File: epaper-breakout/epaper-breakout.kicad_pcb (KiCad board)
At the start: 2 copper layers, 81.3 x 69.8 mm, 63 parts, among them J1 ED097OC4, J2 USB_B_Micro, J3 Conn_01x10, Q1 IRLML6402, SW1 RESET, SW2 BOOT, U1 LT1086-3.3, U2 LT1945, U3 L7915, U4 L7815, U5 ESP32-WROOM-32, U6 CH330N, U7 LM358

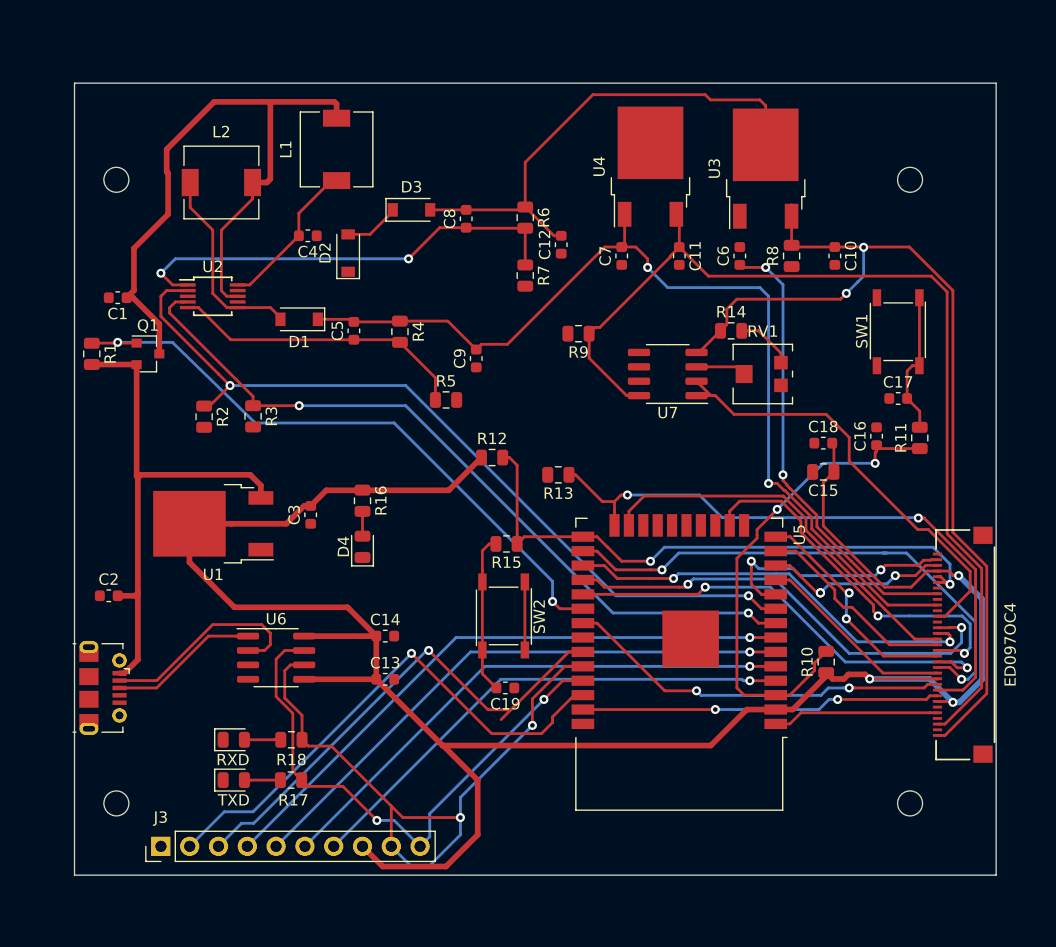
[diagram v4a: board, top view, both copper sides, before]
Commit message: copper pour and ground connections
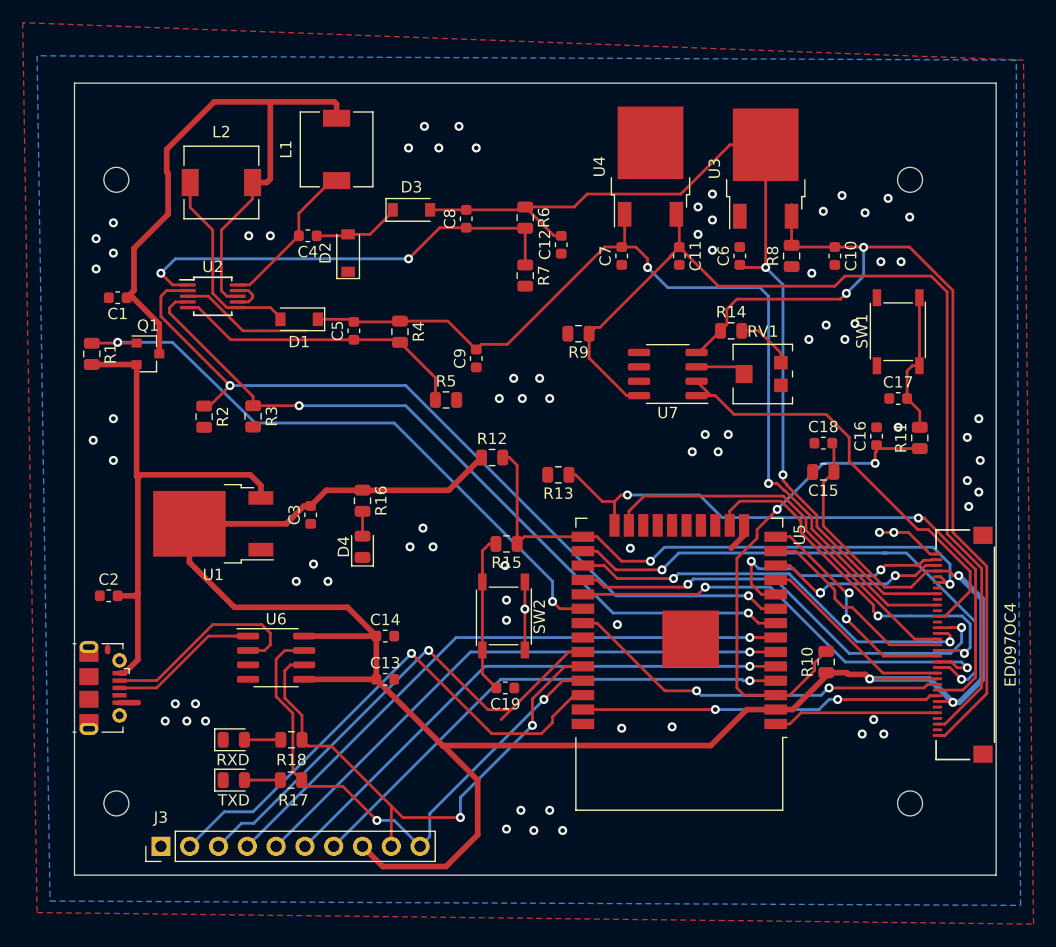
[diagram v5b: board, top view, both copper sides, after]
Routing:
- net GND: track 20.7 -> 45.7 mm, vias 0 -> 76
- net /USB_TXD: track 57.3 -> 47.8 mm
- net /-20V: track 84.4 -> 87.2 mm
- net Net-(C4-Pad1): track 4.92 -> 7.74 mm
- net /15V: track 88.7 -> 89.5 mm
- added copper zone on B.Cu, net GND
- added copper zone on F.Cu, net GND

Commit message: add silk hints
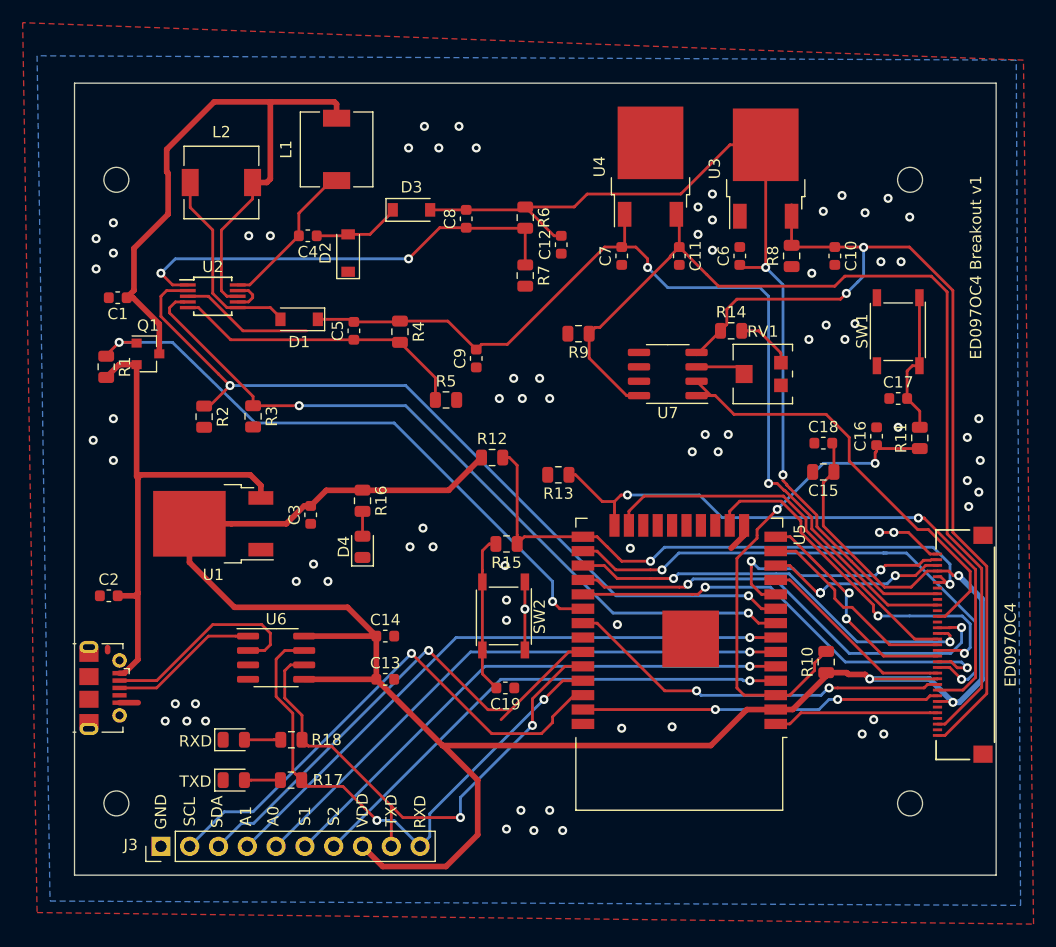
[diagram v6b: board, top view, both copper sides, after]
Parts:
- moved R1 1.71 mm to (54.1, -103.5)
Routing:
- net /5V: track 46.5 -> 45.7 mm
- net /~SMPS_CTRL: track 55.8 -> 55.1 mm
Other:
- board text added: "A0"
- board text added: "A1"
- board text added: "ED097OC4 Breakout v1"
- board text added: "GND"
- board text added: "RXD"
- board text added: "S1"
- board text added: "S2"
- board text added: "SCL"
- board text added: "SDA"
- board text added: "TXD"
- board text added: "VDD"
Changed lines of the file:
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@@
   (general
     (thickness 1.6)
-    (drawings 4)
-    (tracks 780)
+    (drawings 38)
+    (tracks 783)
     (zones 0)
     (modules 63)
@@
     (tags resistor)
     (attr smd)
-    (fp_text reference R18 (at 0 1.778) (layer F.SilkS)
+    (fp_text reference R18 (at 3.0965 0) (layer F.SilkS)
       (effects (font (size 1 1) (thickness 0.15)))
     )
@@
     (tags resistor)
     (attr smd)
-    (fp_text reference R17 (at 0.2055 1.778) (layer F.SilkS)
+    (fp_text reference R17 (at 3.2535 0) (layer F.SilkS)
       (effects (font (size 1 1) (thickness 0.15)))
     )
@@
   )
   (module Resistor_SMD:R_0805_2012Metric (layer F.Cu)
-    (at 52.832 -104.648 270)
+    (at 54.102 -103.505 270)
     (descr "Resistor SMD 0805 (2012 Metric), square (rectangular) end terminal, IPC_7351 nominal, (Body size source: https://docs.google.com/spreadsheets/d/1BsfQQcO9C6DZCsRaXUlFlo91Tg2WpOkGARC1WS5S8t0/edit?usp=sharing), generated with kicad-footprint-generator")
     (tags resistor)
@@
     (descr "Through hole straight pin header, 1x10, 2.54mm pitch, single row")
     (tags "Through hole pin header THT 1x10 2.54mm single row")
-    (fp_text reference J3 (at 2.54 0 180) (layer F.SilkS)
+    (fp_text reference J3 (at 0.127 -2.667 180) (layer F.SilkS)
       (effects (font (size 1 1) (thickness 0.15)))
     )
@@
     (tags diode)
     (attr smd)
-    (fp_text reference RXD (at -0.0785 1.778) (layer F.SilkS)
+    (fp_text reference RXD (at -3.3805 0.127) (layer F.SilkS)
       (effects (font (size 1 1) (thickness 0.15)))
     )
@@
     (tags diode)
     (attr smd)
-    (fp_text reference TXD (at 0 1.778) (layer F.SilkS)
+    (fp_text reference TXD (at -3.3805 0.127) (layer F.SilkS)
       (effects (font (size 1 1) (thickness 0.15)))
     )
@@
     )
   )
+  (gr_text RXD (at 81.788 -64.262 90) (layer F.SilkS)
+    (effects (font (size 1 1) (thickness 0.15)))
+  )
+  (gr_text TXD (at 79.248 -64.389 90) (layer F.SilkS)
+    (effects (font (size 1 1) (thickness 0.15)))
+  )
+  (gr_text VDD (at 76.708 -64.389 90) (layer F.SilkS)
+    (effects (font (size 1 1) (thickness 0.15)))
+  )
+  (gr_text S2 (at 74.168 -63.881 90) (layer F.SilkS)
+    (effects (font (size 1 1) (thickness 0.15)))
+  )
+  (gr_text S1 (at 71.628 -63.881 90) (layer F.SilkS)
+    (effects (font (size 1 1) (thickness 0.15)))
+  )
+  (gr_text A0 (at 68.834 -63.881 90) (layer F.SilkS)
+    (effects (font (size 1 1) (thickness 0.15)))
+  )
+  (gr_text A1 (at 66.421 -63.881 90) (layer F.SilkS)
+    (effects (font (size 1 1) (thickness 0.15)))
+  )
+  (gr_text SDA (at 63.881 -64.262 90) (layer F.SilkS)
+    (effects (font (size 1 1) (thickness 0.15)))
+  )
+  (gr_text SCL (at 61.468 -64.262 90) (layer F.SilkS)
+    (effects (font (size 1 1) (thickness 0.15)))
+  )
+  (gr_text "GND\n" (at 58.928 -64.262 90) (layer F.SilkS)
+    (effects (font (size 1 1) (thickness 0.15)))
+  )
+  (gr_line (start 65.532 -83.058) (end 59.944 -82.55) (layer B.SilkS) (width 0.12))
+  (gr_line (start 65.532 -83.058) (end 72.39 -82.55) (layer B.SilkS) (width 0.12))
+  (gr_line (start 65.024 -90.932) (end 65.151 -92.329) (layer B.SilkS) (width 0.12))
+  (gr_line (start 62.357 -90.805) (end 60.325 -90.551) (layer B.SilkS) (width 0.12))
+  (gr_line (start 60.706 -92.456) (end 59.055 -92.583) (layer B.SilkS) (width 0.12))
+  (gr_line (start 62.357 -90.805) (end 60.706 -92.456) (layer B.SilkS) (width 0.12))
+  (gr_line (start 69.723 -91.313) (end 70.231 -92.71) (layer B.SilkS) (width 0.12))
+  (gr_line (start 67.183 -90.424) (end 69.723 -91.313) (layer B.SilkS) (width 0.12))
+  (gr_line (start 68.834 -92.329) (end 69.977 -94.996) (layer B.SilkS) (width 0.12))
+  (gr_line (start 65.405 -93.218) (end 64.516 -94.996) (layer B.SilkS) (width 0.12))
+  (gr_line (start 63.246 -93.091) (end 63.119 -95.631) (layer B.SilkS) (width 0.12))
+  (gr_line (start 65.024 -90.932) (end 63.246 -93.091) (layer B.SilkS) (width 0.12))
+  (gr_line (start 65.659 -87.884) (end 65.024 -90.932) (layer B.SilkS) (width 0.12))
+  (gr_line (start 68.834 -92.329) (end 67.945 -94.361) (layer B.SilkS) (width 0.12))
+  (gr_line (start 67.183 -90.297) (end 68.834 -92.329) (layer B.SilkS) (width 0.12))
+  (gr_line (start 65.405 -93.218) (end 66.421 -95.25) (layer B.SilkS) (width 0.12))
+  (gr_line (start 67.183 -90.297) (end 65.405 -93.218) (layer B.SilkS) (width 0.12))
+  (gr_line (start 65.659 -87.884) (end 67.183 -90.297) (layer B.SilkS) (width 0.12))
+  (gr_line (start 61.722 -94.361) (end 61.087 -96.393) (layer B.SilkS) (width 0.12))
+  (gr_line (start 61.722 -94.361) (end 62.992 -97.409) (layer B.SilkS) (width 0.12))
+  (gr_line (start 62.357 -90.805) (end 61.722 -94.361) (layer B.SilkS) (width 0.12))
+  (gr_line (start 65.659 -87.884) (end 62.357 -90.805) (layer B.SilkS) (width 0.12))
+  (gr_line (start 65.532 -83.058) (end 65.659 -87.884) (layer B.SilkS) (width 0.12))
+  (gr_text "ED097OC4 Breakout v1" (at 130.81 -112.268 90) (layer F.SilkS)
+    (effects (font (size 1 1) (thickness 0.15)))
+  )
   (gr_line (start 51.308 -128.524) (end 132.588 -128.524) (layer Edge.Cuts) (width 0.1))
   (gr_line (start 51.308 -58.674) (end 51.308 -128.524) (layer Edge.Cuts) (width 0.1))
   (gr_line (start 132.588 -58.674) (end 51.308 -58.674) (layer Edge.Cuts) (width 0.1))
   (gr_line (start 132.588 -128.524) (end 132.588 -58.674) (layer Edge.Cuts) (width 0.1))
-  (segment (start 54.229 -78.74) (end 54.229 -78.385) (width 0.5) (layer F.Cu) (net 0) (status 1000000))
+  (segment (start 54.229 -78.74) (end 54.229 -78.385) (width 0.5) (layer F.Cu) (net 0))
   (segment (start 126.7627 -72.994002) (end 127.4191 -72.994002) (width 0.25) (layer F.Cu) (net 1))
   (segment (start 114.398 -72.009) (end 115.383002 -72.994002) (width 0.25) (layer F.Cu) (net 1))
@@
   (segment (start 56.896 -93.726) (end 57.15 -93.98) (width 0.5) (layer F.Cu) (net 3))
   (segment (start 56.7725 -103.7105) (end 56.785 -103.698) (width 0.5) (layer F.Cu) (net 3))
-  (segment (start 52.832 -103.7105) (end 56.7725 -103.7105) (width 0.5) (layer F.Cu) (net 3))
   (segment (start 56.785 -93.837) (end 56.785 -103.698) (width 0.5) (layer F.Cu) (net 3))
   (segment (start 56.896 -93.726) (end 56.785 -93.837) (width 0.5) (layer F.Cu) (net 3))
@@
   (segment (start 56.896 -77.677) (end 56.896 -83.566) (width 0.5) (layer F.Cu) (net 3))
   (segment (start 56.896 -83.566) (end 56.896 -93.726) (width 0.5) (layer F.Cu) (net 3))
+  (segment (start 55.2325 -103.698) (end 54.102 -102.5675) (width 0.5) (layer F.Cu) (net 3))
+  (segment (start 56.785 -103.698) (end 55.2325 -103.698) (width 0.5) (layer F.Cu) (net 3))
   (segment (start 127.401362 -75.976263) (end 127.4191 -75.994001) (width 0.25) (layer F.Cu) (net 4))
   (segment (start 126.51641 -85.494) (end 125.09641 -84.074) (width 0.25) (layer F.Cu) (net 4))
@@
   (segment (start 67.252998 -98.552) (end 59.944 -105.664) (width 0.25) (layer B.Cu) (net 56))
   (segment (start 79.502 -98.552) (end 67.252998 -98.552) (width 0.25) (layer B.Cu) (net 56))
-  (via (at 55.118 -105.664) (size 0.8) (drill 0.4) (layers F.Cu B.Cu) (net 56))
+  (via (at 55.245 -105.664) (size 0.8) (drill 0.4) (layers F.Cu B.Cu) (net 56))
   (segment (start 56.851 -105.664) (end 56.785 -105.598) (width 0.25) (layer F.Cu) (net 56))
-  (segment (start 52.8445 -105.598) (end 52.832 -105.5855) (width 0.25) (layer F.Cu) (net 56))
-  (segment (start 56.785 -105.598) (end 52.8445 -105.598) (width 0.25) (layer F.Cu) (net 56))
   (segment (start 59.944 -105.664) (end 55.118 -105.664) (width 0.25) (layer B.Cu) (net 56))
+  (segment (start 54.102 -104.521) (end 55.245 -105.664) (width 0.25) (layer F.Cu) (net 56))
+  (segment (start 54.102 -104.4425) (end 54.102 -104.521) (width 0.25) (layer F.Cu) (net 56))
+  (segment (start 56.719 -105.664) (end 56.785 -105.598) (width 0.25) (layer F.Cu) (net 56))
+  (segment (start 55.245 -105.664) (end 56.719 -105.664) (width 0.25) (layer F.Cu) (net 56))
   (segment (start 111.898 -82.169) (end 110.755 -83.312) (width 0.25) (layer F.Cu) (net 57))
   (segment (start 113.148 -82.169) (end 111.898 -82.169) (width 0.25) (layer F.Cu) (net 57))

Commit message: new copper pour
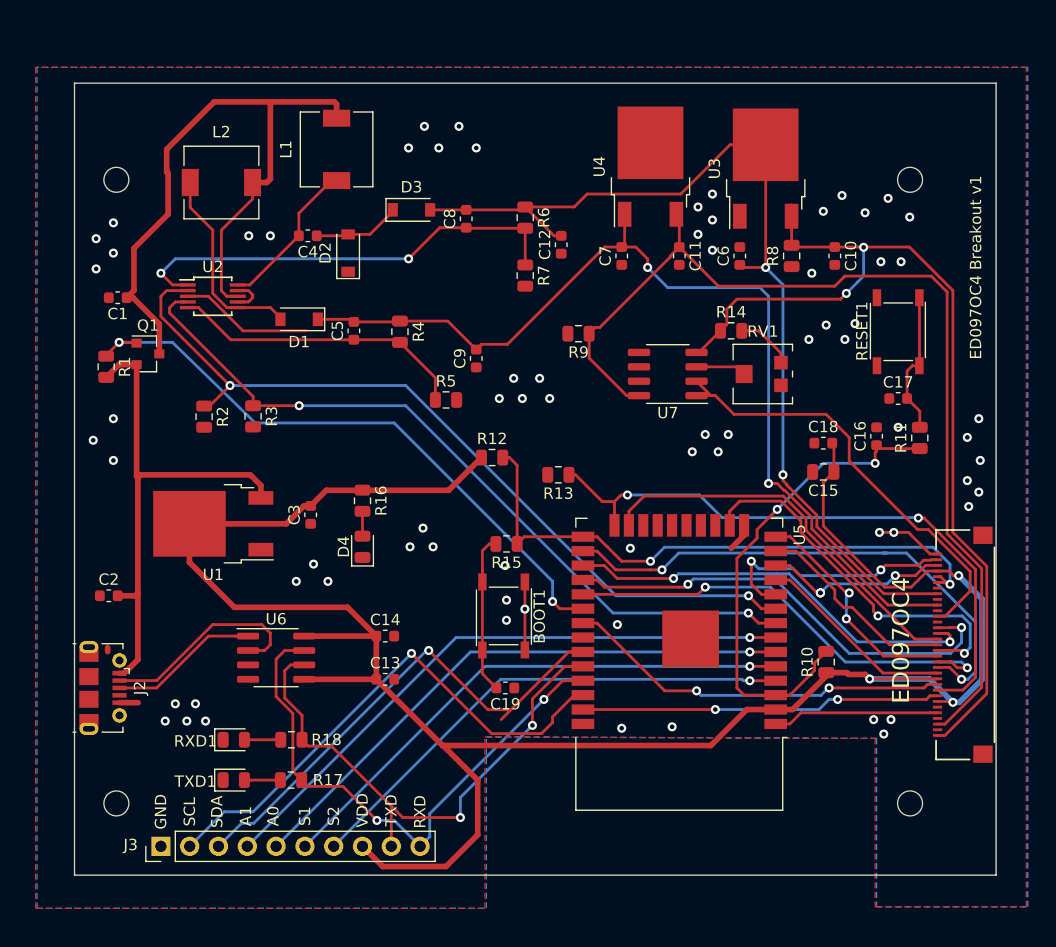
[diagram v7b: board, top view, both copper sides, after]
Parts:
- BOOT1: renamed from SW2; value BOOT -> SW2
- J1: value ED097OC4 -> XF2M-3315-1A
- J2: value USB_B_Micro -> C10418
- RESET1: renamed from SW1; value RESET -> SW1
- RXD1: renamed from RXD; value RXD -> LED2
- TXD1: renamed from TXD; value TXD -> LED1
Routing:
- net GND: vias 76 -> 71
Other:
- board text added: "ED097OC4"
